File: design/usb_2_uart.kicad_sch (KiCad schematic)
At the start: 12 parts, among them Q1 SS8050, Q2 SS8050, U4 CH340G, Y1 12MHz

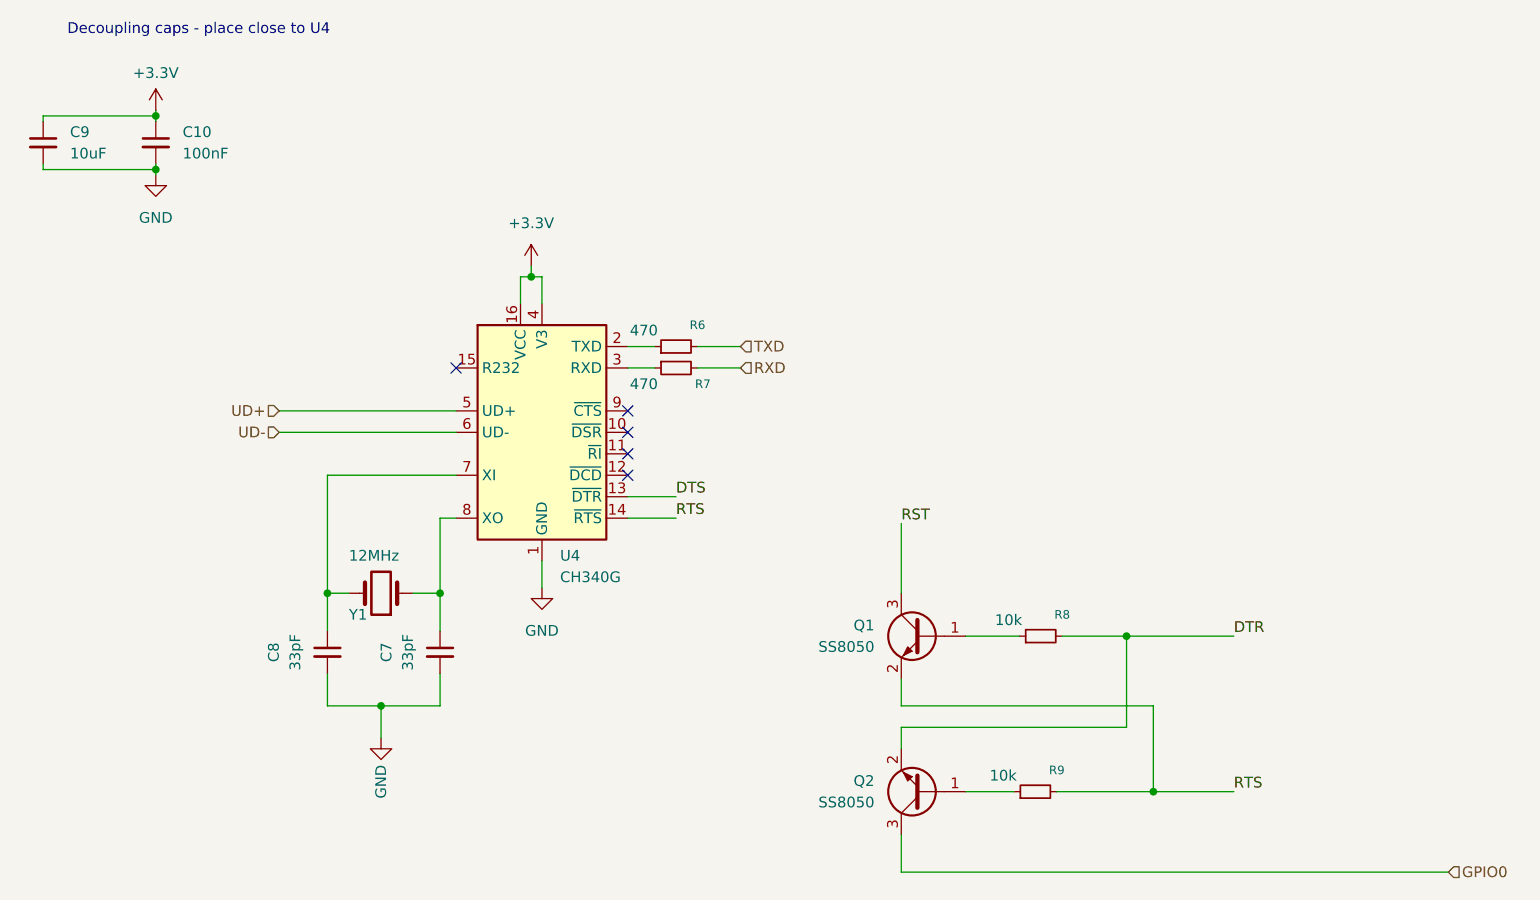
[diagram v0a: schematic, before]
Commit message: Added some more sheets, new board layout
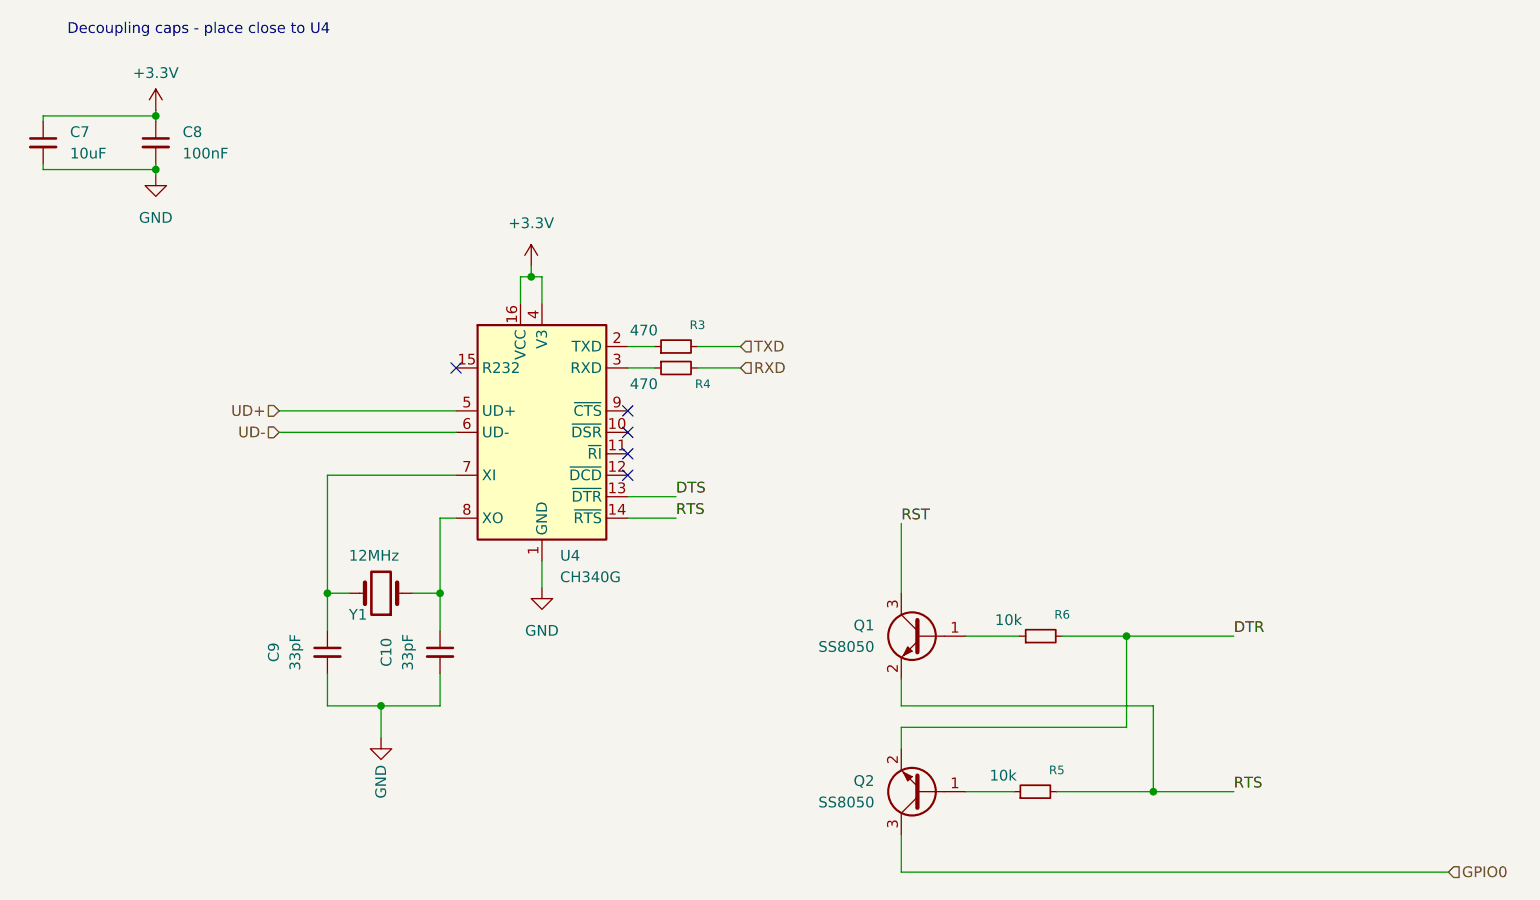
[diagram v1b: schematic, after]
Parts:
- renumbered C7 to C10, C9 to C7, C10 to C8, C8 to C9, R6 to R3, R7 to R4, R9 to R5, R8 to R6
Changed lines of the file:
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@@
 		(dnp no)
 		(fields_autoplaced yes)
-		(property "Reference" "C8"
+		(property "Reference" "C9"
 			(at 105.41 119.3864 90)
 			(effects
@@
 			(project "RocketClock"
 				(path "/e36fbef8-3f03-40ce-b8c1-50d21e162c91/18568fcc-63f9-46c1-91a1-85cb52dff52c"
-					(reference "C8")
+					(reference "C9")
 					(unit 1)
 				)
@@
 		(dnp no)
 		(fields_autoplaced yes)
-		(property "Reference" "C7"
+		(property "Reference" "C10"
 			(at 118.745 119.3864 90)
 			(effects
@@
 			(project ""
 				(path "/e36fbef8-3f03-40ce-b8c1-50d21e162c91/18568fcc-63f9-46c1-91a1-85cb52dff52c"
-					(reference "C7")
+					(reference "C10")
 					(unit 1)
 				)
@@
 		(on_board yes)
 		(dnp no)
-		(property "Reference" "R7"
+		(property "Reference" "R4"
 			(at 156.21 87.63 90)
 			(effects
@@
 			(project "RocketClock"
 				(path "/e36fbef8-3f03-40ce-b8c1-50d21e162c91/18568fcc-63f9-46c1-91a1-85cb52dff52c"
-					(reference "R7")
+					(reference "R4")
 					(unit 1)
 				)
@@
 		(dnp no)
 		(fields_autoplaced yes)
-		(property "Reference" "#PWR023"
+		(property "Reference" "#PWR019"
 			(at 91.44 69.215 0)
 			(effects
@@
 			(project "RocketClock"
 				(path "/e36fbef8-3f03-40ce-b8c1-50d21e162c91/18568fcc-63f9-46c1-91a1-85cb52dff52c"
-					(reference "#PWR023")
+					(reference "#PWR019")
 					(unit 1)
 				)
@@
 		(dnp no)
 		(fields_autoplaced yes)
-		(property "Reference" "C9"
+		(property "Reference" "C7"
 			(at 81.28 57.7912 0)
 			(effects
@@
 			(project "RocketClock"
 				(path "/e36fbef8-3f03-40ce-b8c1-50d21e162c91/18568fcc-63f9-46c1-91a1-85cb52dff52c"
-					(reference "C9")
+					(reference "C7")
 					(unit 1)
 				)
@@
 		(on_board yes)
 		(dnp no)
-		(property "Reference" "R8"
+		(property "Reference" "R6"
 			(at 198.755 114.935 90)
 			(effects
@@
 			(project "RocketClock"
 				(path "/e36fbef8-3f03-40ce-b8c1-50d21e162c91/18568fcc-63f9-46c1-91a1-85cb52dff52c"
-					(reference "R8")
+					(reference "R6")
 					(unit 1)
 				)
@@
 		(dnp no)
 		(fields_autoplaced yes)
-		(property "Reference" "#PWR022"
+		(property "Reference" "#PWR018"
 			(at 91.44 59.055 0)
 			(effects
@@
 			(project "RocketClock"
 				(path "/e36fbef8-3f03-40ce-b8c1-50d21e162c91/18568fcc-63f9-46c1-91a1-85cb52dff52c"
-					(reference "#PWR022")
+					(reference "#PWR018")
 					(unit 1)
 				)
@@
 		(on_board yes)
 		(dnp no)
-		(property "Reference" "R9"
+		(property "Reference" "R5"
 			(at 198.12 133.35 90)
 			(effects
@@
 			(project "RocketClock"
 				(path "/e36fbef8-3f03-40ce-b8c1-50d21e162c91/18568fcc-63f9-46c1-91a1-85cb52dff52c"
-					(reference "R9")
+					(reference "R5")
 					(unit 1)
 				)
@@
 		(dnp no)
 		(fields_autoplaced yes)
-		(property "Reference" "#PWR018"
+		(property "Reference" "#PWR022"
 			(at 137.16 118.11 0)
 			(effects
@@
 			(project ""
 				(path "/e36fbef8-3f03-40ce-b8c1-50d21e162c91/18568fcc-63f9-46c1-91a1-85cb52dff52c"
-					(reference "#PWR018")
+					(reference "#PWR022")
 					(unit 1)
 				)
@@
 		(on_board yes)
 		(dnp no)
-		(property "Reference" "R6"
+		(property "Reference" "R3"
 			(at 155.575 80.645 90)
 			(effects
@@
 			(project ""
 				(path "/e36fbef8-3f03-40ce-b8c1-50d21e162c91/18568fcc-63f9-46c1-91a1-85cb52dff52c"
-					(reference "R6")
+					(reference "R3")
 					(unit 1)
 				)
@@
 		(dnp no)
 		(fields_autoplaced yes)
-		(property "Reference" "#PWR019"
+		(property "Reference" "#PWR021"
 			(at 135.89 77.47 0)
 			(effects
@@
 			(project ""
 				(path "/e36fbef8-3f03-40ce-b8c1-50d21e162c91/18568fcc-63f9-46c1-91a1-85cb52dff52c"
-					(reference "#PWR019")
+					(reference "#PWR021")
 					(unit 1)
 				)
@@
 		(dnp no)
 		(fields_autoplaced yes)
-		(property "Reference" "#PWR021"
+		(property "Reference" "#PWR020"
 			(at 118.11 135.89 0)
 			(effects
@@
 			(project ""
 				(path "/e36fbef8-3f03-40ce-b8c1-50d21e162c91/18568fcc-63f9-46c1-91a1-85cb52dff52c"
-					(reference "#PWR021")
+					(reference "#PWR020")
 					(unit 1)
 				)
@@
 		(dnp no)
 		(fields_autoplaced yes)
-		(property "Reference" "C10"
+		(property "Reference" "C8"
 			(at 94.615 57.7912 0)
 			(effects
@@
 			(project "RocketClock"
 				(path "/e36fbef8-3f03-40ce-b8c1-50d21e162c91/18568fcc-63f9-46c1-91a1-85cb52dff52c"
-					(reference "C10")
-					(unit 1)
-				)
+					(reference "C8")
+					(unit 1)
+				)

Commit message: layout mostly done, schematic is done, need to generate new updated pdf
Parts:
- Y1: footprint (none) -> Crystal:Crystal_SMD_3225-4Pin_3.2x2.5mm_HandSoldering
- renumbered R3 to R5, R4 to R6, R6 to R7, R5 to R8
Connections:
- net DTS is gone; now on net DTR: U4.13 (~{DTR})
- net RST renamed ~{RST}
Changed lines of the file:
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@@
+	(wire
+		(pts
+			(xy 179.705 104.775) (xy 179.705 112.395)
+		)
+		(stroke
+			(width 0)
+			(type default)
+		)
+	)
 	(wire
 		(pts
@@
 	(wire
 		(pts
-			(xy 179.705 104.14) (xy 179.705 112.395)
-		)
-		(stroke
-			(width 0)
-			(type default)
-		)
-	)
-	(wire
-		(pts
 			(xy 147.32 83.185) (xy 150.495 83.185)
 		)
@@
 		(pts
 			(xy 206.375 128.27) (xy 206.375 117.475)
+		)
+		(stroke
+			(width 0)
+			(type default)
+		)
+	)
+	(wire
+		(pts
+			(xy 217.17 104.775) (xy 179.705 104.775)
 		)
 		(stroke
@@
 		)
 	)
-	(label "DTS"
+	(label "DTR"
 		(at 153.035 100.965 0)
-		(effects
-			(font
-				(size 1.27 1.27)
-			)
-			(justify left bottom)
-		)
-	)
-	(label "RST"
-		(at 179.705 104.14 0)
 		(effects
 			(font
@@
 		(shape input)
 		(at 160.655 85.725 0)
+		(effects
+			(font
+				(size 1.27 1.27)
+			)
+			(justify left)
+		)
+	)
+	(hierarchical_label "~{RST}"
+		(shape input)
+		(at 217.17 104.775 0)
 		(effects
 			(font
@@
 		(on_board yes)
 		(dnp no)
-		(property "Reference" "R4"
+		(property "Reference" "R6"
 			(at 156.21 87.63 90)
 			(effects
@@
 			(project "RocketClock"
 				(path "/e36fbef8-3f03-40ce-b8c1-50d21e162c91/18568fcc-63f9-46c1-91a1-85cb52dff52c"
-					(reference "R4")
+					(reference "R6")
 					(unit 1)
 				)
@@
 		(dnp no)
 		(fields_autoplaced yes)
-		(property "Reference" "#PWR019"
+		(property "Reference" "#PWR021"
 			(at 91.44 69.215 0)
 			(effects
@@
 			(project "RocketClock"
 				(path "/e36fbef8-3f03-40ce-b8c1-50d21e162c91/18568fcc-63f9-46c1-91a1-85cb52dff52c"
-					(reference "#PWR019")
+					(reference "#PWR021")
 					(unit 1)
 				)
@@
 		(on_board yes)
 		(dnp no)
-		(property "Reference" "R6"
+		(property "Reference" "R7"
 			(at 198.755 114.935 90)
 			(effects
@@
 			(project "RocketClock"
 				(path "/e36fbef8-3f03-40ce-b8c1-50d21e162c91/18568fcc-63f9-46c1-91a1-85cb52dff52c"
-					(reference "R6")
+					(reference "R7")
 					(unit 1)
 				)
@@
 		(dnp no)
 		(fields_autoplaced yes)
-		(property "Reference" "#PWR018"
+		(property "Reference" "#PWR020"
 			(at 91.44 59.055 0)
 			(effects
@@
 			(project "RocketClock"
 				(path "/e36fbef8-3f03-40ce-b8c1-50d21e162c91/18568fcc-63f9-46c1-91a1-85cb52dff52c"
-					(reference "#PWR018")
+					(reference "#PWR020")
 					(unit 1)
 				)
@@
 		(on_board yes)
 		(dnp no)
-		(property "Reference" "R5"
+		(property "Reference" "R8"
 			(at 198.12 133.35 90)
 			(effects
@@
 			(project "RocketClock"
 				(path "/e36fbef8-3f03-40ce-b8c1-50d21e162c91/18568fcc-63f9-46c1-91a1-85cb52dff52c"
-					(reference "R5")
+					(reference "R8")
 					(unit 1)
 				)
@@
 		(dnp no)
 		(fields_autoplaced yes)
-		(property "Reference" "#PWR022"
+		(property "Reference" "#PWR023"
 			(at 137.16 118.11 0)
 			(effects
@@
 			(project ""
 				(path "/e36fbef8-3f03-40ce-b8c1-50d21e162c91/18568fcc-63f9-46c1-91a1-85cb52dff52c"
-					(reference "#PWR022")
+					(reference "#PWR023")
 					(unit 1)
 				)
@@
 			)
 		)
-		(property "Footprint" ""
+		(property "Footprint" "Crystal:Crystal_SMD_3225-4Pin_3.2x2.5mm_HandSoldering"
 			(at 118.11 112.395 0)
 			(effects
@@
 		(on_board yes)
 		(dnp no)
-		(property "Reference" "R3"
+		(property "Reference" "R5"
 			(at 155.575 80.645 90)
 			(effects
@@
 			(project ""
 				(path "/e36fbef8-3f03-40ce-b8c1-50d21e162c91/18568fcc-63f9-46c1-91a1-85cb52dff52c"
-					(reference "R3")
+					(reference "R5")
 					(unit 1)
 				)
@@
 		(dnp no)
 		(fields_autoplaced yes)
-		(property "Reference" "#PWR021"
+		(property "Reference" "#PWR022"
 			(at 135.89 77.47 0)
 			(effects
@@
 			(project ""
 				(path "/e36fbef8-3f03-40ce-b8c1-50d21e162c91/18568fcc-63f9-46c1-91a1-85cb52dff52c"
-					(reference "#PWR021")
+					(reference "#PWR022")
 					(unit 1)
 				)
@@
 		(dnp no)
 		(fields_autoplaced yes)
-		(property "Reference" "#PWR020"
+		(property "Reference" "#PWR024"
 			(at 118.11 135.89 0)
 			(effects
@@
 			(project ""
 				(path "/e36fbef8-3f03-40ce-b8c1-50d21e162c91/18568fcc-63f9-46c1-91a1-85cb52dff52c"
-					(reference "#PWR020")
+					(reference "#PWR024")
 					(unit 1)
 				)
